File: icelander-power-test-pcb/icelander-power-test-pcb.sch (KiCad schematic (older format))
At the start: 24 parts

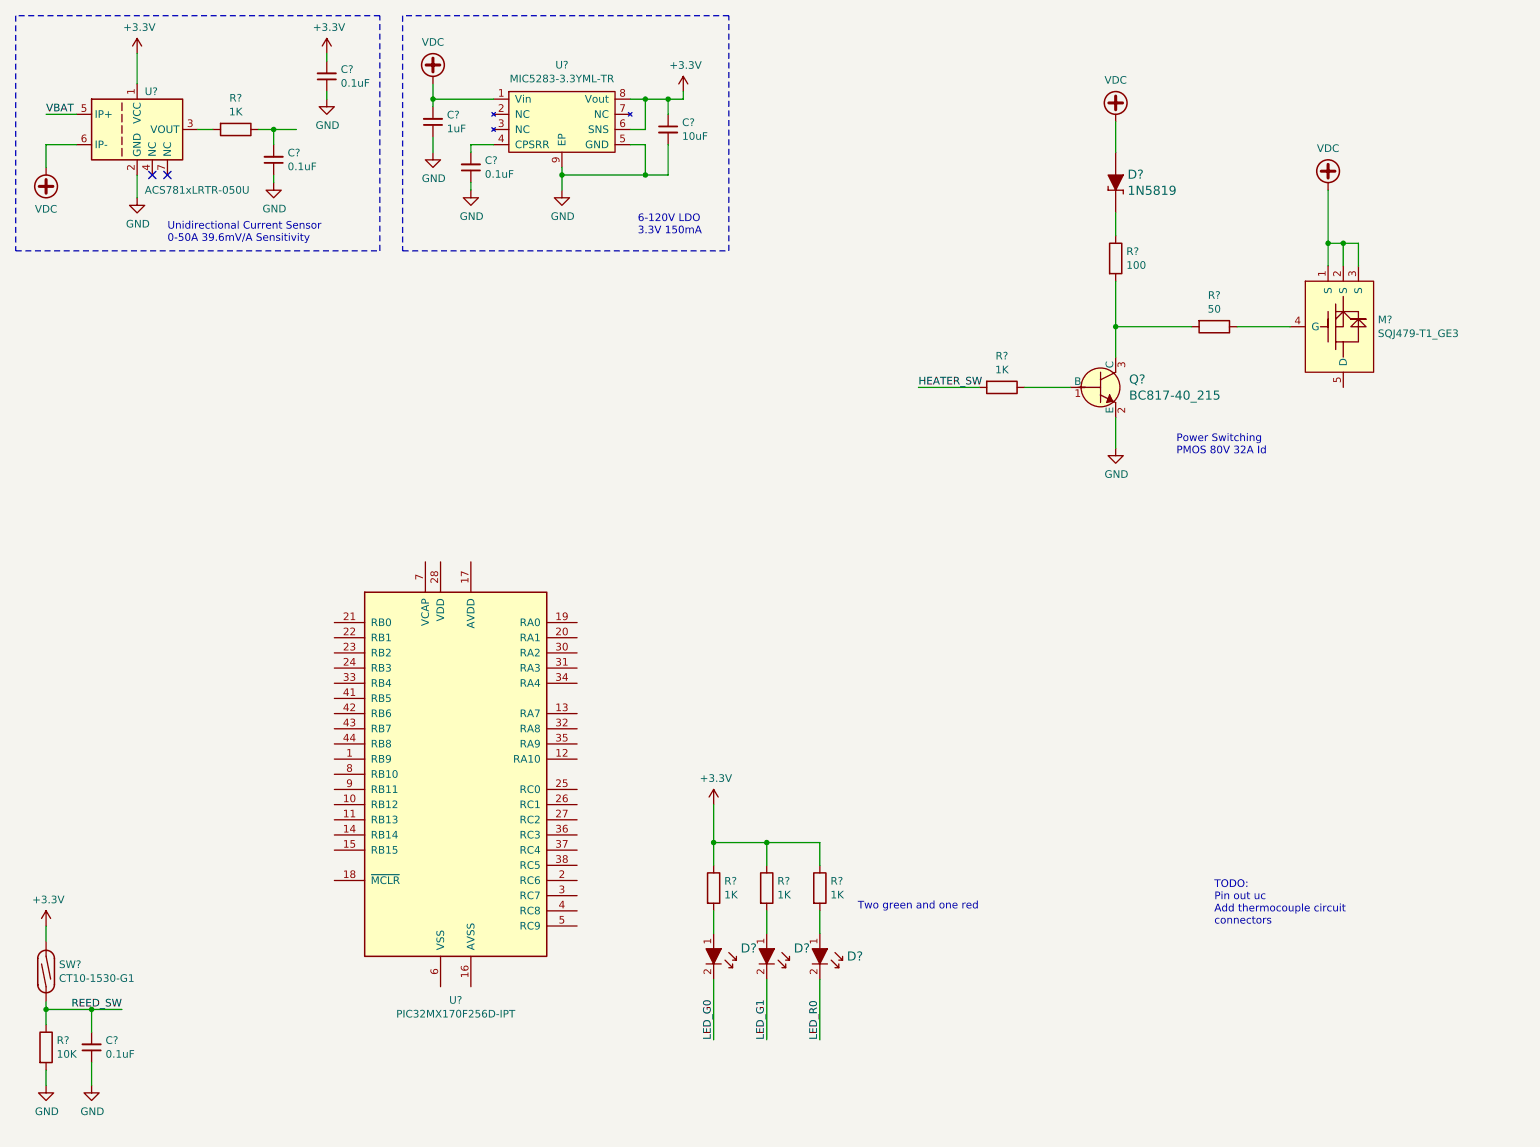
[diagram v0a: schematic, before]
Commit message: soft schematic finished
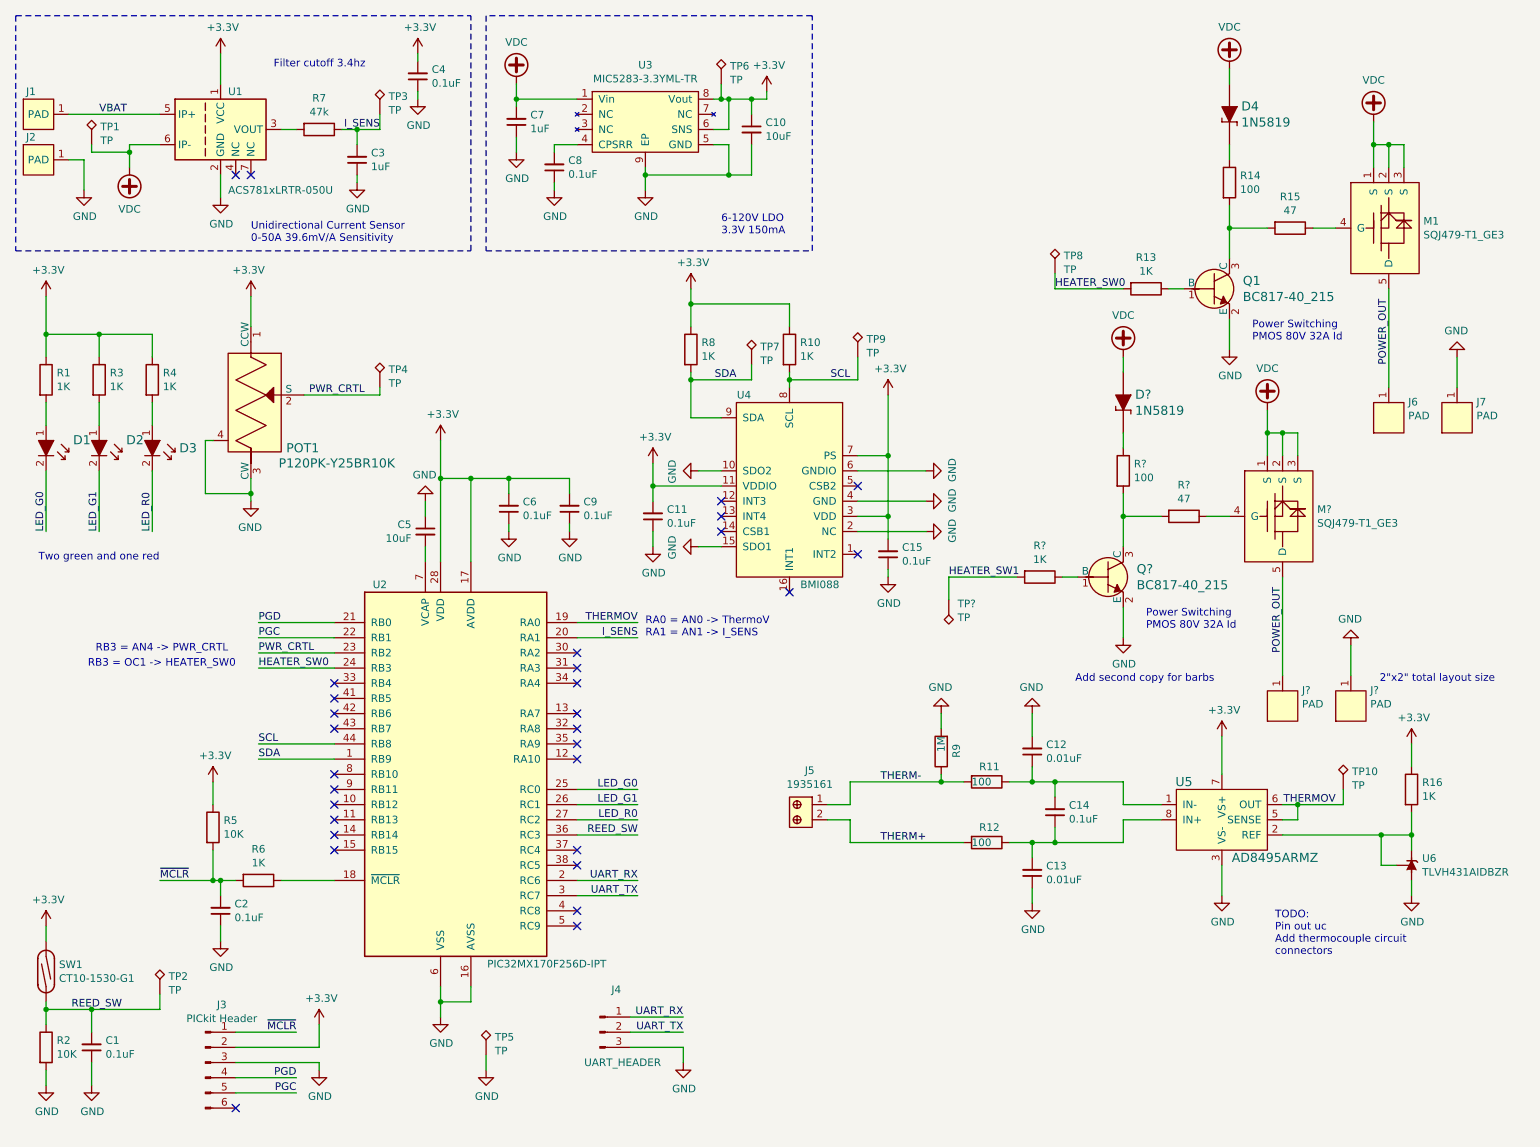
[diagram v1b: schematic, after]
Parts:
- removed C?: 0.1uF, Capacitor_SMD:C_0805_2012Metric_Pad1.15x1.40mm_HandSolder, symbol Device:C_Small
- added C11, C14, C15, C2, C6, C9: 0.1uF, Capacitor_SMD:C_0805_2012Metric_Pad1.15x1.40mm_HandSolder, symbol Device:C_Small
- added C12, C13: 0.01uF, Capacitor_SMD:C_0805_2012Metric_Pad1.15x1.40mm_HandSolder, symbol Device:C_Small
- added C3: 1uF, Capacitor_SMD:C_0805_2012Metric_Pad1.15x1.40mm_HandSolder, symbol Device:C_Small
- added C5: 10uF, Capacitor_SMD:C_0805_2012Metric_Pad1.15x1.40mm_HandSolder, symbol Device:C_Small
- added D?: 1N5819, digikey-footprints:DO-41, symbol dk_Diodes-Rectifiers-Single:1N5819
- added J1, J2, J6, J7, J? (x2): PAD, icelander-power-test-pcb:PowerPad, symbol IceLander-Power-test-pcb:PAD
- added J3: PICkit Header, Connector_PinHeader_2.54mm:PinHeader_1x06_P2.54mm_Vertical, symbol Connector:Conn_01x06_Male
- added J4: UART_HEADER, Connector_PinHeader_2.54mm:PinHeader_1x03_P2.54mm_Vertical, symbol Connector:Conn_01x03_Male
- added J5: 1935161, digikey-footprints:Terminal_Block_D1.3mm_P5mm, symbol dk_Terminal-Blocks-Wire-to-Board:1935161
- added M?: SQJ479-T1_GE3, Package_SO:PowerPAK_SO-8_Single, symbol IceLander-Power-test-pcb:SQJ479-T1_GE3
- added POT1: P120PK-Y25BR10K, digikey-footprints:Potentiometer_P120PK-Y25BR10K, symbol dk_Rotary-Potentiometers-Rheostats:P120PK-Y25BR10K
- added Q?: BC817-40_215, digikey-footprints:SOT-23-3, symbol dk_Transistors-Bipolar-BJT-Single:BC817-40_215
- added R10, R16, R6, R8, R?: 1K, Resistor_SMD:R_0805_2012Metric_Pad1.15x1.40mm_HandSolder, symbol Device:R
- added R11, R12, R?: 100, Resistor_SMD:R_0805_2012Metric_Pad1.15x1.40mm_HandSolder, symbol Device:R
- added R5: 10K, Resistor_SMD:R_0805_2012Metric_Pad1.15x1.40mm_HandSolder, symbol Device:R
- added R9: 1M, Resistor_SMD:R_0805_2012Metric_Pad1.15x1.40mm_HandSolder, symbol Device:R
- added R?: 47, Resistor_SMD:R_0805_2012Metric_Pad1.15x1.40mm_HandSolder, symbol Device:R
- added TP1, TP10, TP2, TP3, TP4, TP5, TP6, TP7, TP8, TP9, TP?: TP, OSU_SIM_BASIC:Keystone_5019, symbol Connector:TestPoint_Alt
- added U4: BMI088, icelander-power-test-pcb:BMI088-LGA-16, symbol IceLander-Power-test-pcb:BMI088-Sensor_Motion
- added U5: AD8495ARMZ, digikey-footprints:TSSOP-8_W3mm, symbol dk_Interface-Sensor-and-Detector-Interfaces:AD8495ARMZ
- added U6: TLVH431AIDBZR, Package_TO_SOT_SMD:SOT-23, symbol Reference_Voltage:TL431DBZ
- C1, C4, C8: renamed from C?; Digi-Key_PN (none) -> 399-8000-1-ND
- C10: renamed from C?; Digi-Key_PN (none) -> 1276-2893-1-ND
- C7: renamed from C?; Digi-Key_PN (none) -> 399-1284-1-ND
- R1, R13, R3, R4: renamed from R?; Digi-Key_PN (none) -> 311-1.0KARCT-ND
- R14: renamed from R?; Digi-Key_PN (none) -> P100DACT-ND
- R15: renamed from R?; value 50 -> 47; Digi-Key_PN (none) -> A126371CT-ND
- R2: renamed from R?; Digi-Key_PN (none) -> 311-10.0KCRCT-ND
- R7: renamed from R?; value 1K -> 47k; Digi-Key_PN (none) -> A130144CT-ND
- SW1: renamed from SW?; footprint (none) -> icelander-power-test-pcb:CT10-XXXX-G1
- gave numbers to parts that had none: 9
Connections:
- net HEATER_SW is gone; now on net HEATER_SW0: R13.2
- net +3V3: now also U2.17 (AVDD), U2.28 (VDD), U2.40 (VDD), C11.2, C15.2, C6.2, C9.2, J3.2 (Pin_2), POT1.1 (CCW), R10.1, R16.1, R5.1, R8.1, TP6.1, U4.11 (VDDIO), U4.3 (VDD), U4.7 (PS), U5.7 (VS+)
- net GND: now also U2.16 (AVSS), U2.29 (VSS), U2.39 (VSS), U2.6 (VSS), C11.1, C12.2, C13.1, C15.1, C2.1, C3.1, C5.1, C6.1, C9.1, J2.1, J3.3 (Pin_3), J4.3 (Pin_3), J7.1, J?.1, POT1.3 (CW), POT1.4, Q?.2 (E), R9.2, TP5.1, U4.10 (SDO2), U4.15 (SDO1), U4.2 (NC), U4.4 (GND), U4.6 (GNDIO), U5.3 (VS-), U6.3 (A)
- net LED_G0: now also U2.25 (RC0)
- net LED_G1: now also U2.26 (RC1)
- net LED_R0: now also U2.27 (RC2)
- net REED_SW: now also U2.36 (RC3), TP2.1
- net VBAT: now also J1.1
- net VDC: now also D?.A, M?.1 (S), M?.2 (S), M?.3 (S), TP1.1
- net POWER_OUT: now reaches M1.5 (D)
- net POWER_OUT: now also J6.1, J?.1, M?.5 (D)
- net SDA: now reaches U2.1 (RB9)
- net SDA: now also R8.2, TP7.1, U4.9 (SDA)
- net at U2.18 (~MCLR): now also R6.1
- net THERMOV: now reaches U2.19 (RA0)
- net THERMOV: now also TP10.1, U5.5 (SENSE), U5.6 (OUT)
- net UART_RX: now reaches U2.2 (RC6)
- net UART_RX: now also J4.1 (Pin_1)
- net I_SENS: now reaches U2.20 (RA1)
- net I_SENS: now also R7.1, C3.2, TP3.1
- net PGD: now reaches U2.21 (RB0)
- net PGD: now also J3.4 (Pin_4)
- net PGC: now reaches U2.22 (RB1)
- net PGC: now also J3.5 (Pin_5)
- net PWR_CRTL: now reaches U2.23 (RB2)
- net PWR_CRTL: now also POT1.2 (S), TP4.1
- net HEATER_SW0: now reaches U2.24 (RB3)
- net HEATER_SW0: now also TP8.1
- net UART_TX: now reaches U2.3 (RC7)
- net UART_TX: now also J4.2 (Pin_2)
- net SCL: now reaches U2.44 (RB8)
- net SCL: now also R10.2, TP9.1, U4.8 (SCL)
- net at U2.7 (VCAP): now also C5.2
- new net: R16.2, U5.2 (REF), U6.1 (K), U6.2 (REF)
- new net: C12.1, C14.2, R11.1, U5.1 (IN-)
- new net: C13.2, C14.1, R12.1, U5.8 (IN+)
- new net: M?.4 (G), R?.1
- new net: Q?.1 (B), R?.1
- new net: Q?.3 (C), R?.2, R?.2
- new net: D?.K, R?.1
- new net HEATER_SW1: R?.2, TP?.1
- new net THERM+: J5.2, R12.2
- new net THERM-: J5.1, R11.2, R9.1
- new net ~MCLR: C2.2, J3.1 (Pin_1), R5.2, R6.2
- no-connect marks 2 -> 30
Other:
- note added: "2"x2" total layout size"
- note added: "Add second copy for barbs\n"
- note added: "Filter cutoff 3.4hz\n"
- note added: "RA0 = AN0 -> ThermoV\nRA1 = AN1 -> I_SENS"
- note added: "RB3 = AN4 -> PWR_CRTL"
- note added: "RB3 = OC1 -> HEATER_SW0\n"
- moved on the sheet: C10, C4, C7, C8, D1, D2, D3, D4, M1, Q1, R1, R13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

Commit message: sch finished ready to start layout
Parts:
- removed C10: 10uF, Capacitor_SMD:C_0805_2012Metric_Pad1.15x1.40mm_HandSolder, symbol Device:C_Small
- removed C3, C7: 1uF, Capacitor_SMD:C_0805_2012Metric_Pad1.15x1.40mm_HandSolder, symbol Device:C_Small
- removed C4, C8: 0.1uF, Capacitor_SMD:C_0805_2012Metric_Pad1.15x1.40mm_HandSolder, symbol Device:C_Small
- removed D4, D?: 1N5819, digikey-footprints:DO-41, symbol dk_Diodes-Rectifiers-Single:1N5819
- removed J1, J2, J6, J7, J? (x2): PAD, icelander-power-test-pcb:PowerPad, symbol IceLander-Power-test-pcb:PAD
- removed M1, M?: SQJ479-T1_GE3, Package_SO:PowerPAK_SO-8_Single, symbol IceLander-Power-test-pcb:SQJ479-T1_GE3
- removed Q1, Q?: BC817-40_215, digikey-footprints:SOT-23-3, symbol dk_Transistors-Bipolar-BJT-Single:BC817-40_215
- removed R13, R?: 1K, Resistor_SMD:R_0805_2012Metric_Pad1.15x1.40mm_HandSolder, symbol Device:R
- removed R14, R?: 100, Resistor_SMD:R_0805_2012Metric_Pad1.15x1.40mm_HandSolder, symbol Device:R
- removed R15, R?: 47, Resistor_SMD:R_0805_2012Metric_Pad1.15x1.40mm_HandSolder, symbol Device:R
- removed R7: 47k, Resistor_SMD:R_0805_2012Metric_Pad1.15x1.40mm_HandSolder, symbol Device:R
- removed TP1, TP3, TP6, TP8, TP?: TP, OSU_SIM_BASIC:Keystone_5019, symbol Connector:TestPoint_Alt
- removed U1: ACS781xLRTR-050U, Sensor_Current:Allegro_PSOF-7_4.8x6.4mm_P1.60mm, symbol Sensor_Current:ACS781xLRTR-050U
- removed U3: MIC5283-3.3YML-TR, icelander-power-test-pcb:VDFM-8_EP_3x3mm, symbol IceLander-Power-test-pcb:MIC5283-3.3YML-TR
- renumbered C14 to C10, C5 to C3, C11 to C4, C6 to C5, C9 to C6, C15 to C7, C12 to C8, C13 to C9, J3 to J1, J4 to J2, J5 to J3, R11 to R10, R12 to R11, R16 to R12, R8 to R7, R10 to R8, TP2 to TP1, TP4 to TP2, TP5 to TP3, TP7 to TP4, TP9 to TP5, TP10 to TP6, U2 to U1, U4 to U2, U5 to U3, U6 to U4
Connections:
- net HEATER_SW1: now also U1.41 (RB5)
- net PGOOD: now reaches U1.37 (RC4)
- no-connect marks 30 -> 26
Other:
- note added: "DC Regulation\nPower Switching\nPower Monitoring"
- note added: "RB5 = OC2 -> HEATER_SW1\n"
- note removed: "6-120V LDO\n3.3V 150mA"
- note removed: "Add second copy for barbs\n"
- note removed: "Filter cutoff 3.4hz\n"
- note removed: "Power Switching \nPMOS 80V 32A Id"
- note removed: "Unidirectional Current Sensor\n0-50A 39.6mV/A Sensitivity"
- moved on the sheet: C4, C7, D1, D2, D3, POT1, R1, R3, R4, R7, R8, TP2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

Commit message: swappe uc updated 3d settings
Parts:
- removed U1: PIC32MX170F256D-IPT, Package_QFP:TQFP-44_10x10mm_P0.8mm, symbol MCU_Microchip_PIC32:PIC32MX170F256D-IPT
- added C50, C51, C52, C53, C54, C55, C56: 0.1uF, Capacitor_SMD:C_0805_2012Metric_Pad1.15x1.40mm_HandSolder, symbol Device:C_Small
- added C57: 10uF, Capacitor_SMD:C_0805_2012Metric_Pad1.15x1.40mm_HandSolder, symbol Device:C_Small
- added FB1: BLM18PG121SN1D, Inductor_SMD:L_0603_1608Metric_Pad1.05x0.95mm_HandSolder, symbol dk_Ferrite-Beads-and-Chips:BLM18PG121SN1D
- added S1: GPTS203211B, digikey-footprints:PushButton_12x12mm_THT_GPTS203211B, symbol dk_Pushbutton-Switches:GPTS203211B
- added U1: STM32F030CCTx, Package_QFP:LQFP-48_7x7mm_P0.5mm, symbol MCU_ST_STM32F0:STM32F030CCTx
- added XTAL1: NX3225GD-8MHZ-STD-CRA-3, digikey-footprints:SMD-2_3.2x2.5mm, symbol dk_Crystals:NX3225GD-8MHZ-STD-CRA-3
- C3: value 10uF -> 10pF; Digi-Key_PN 1276-2893-1-ND -> 311-1058-1-ND
- C5: value 0.1uF -> 10pF; Digi-Key_PN 399-8000-1-ND -> 311-1058-1-ND
- J1: value PICkit Header -> SWIO Header
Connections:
- net +3V3: now also C50.2, C51.2, C52.2, C53.2, C54.2, C55.2, C56.2, C57.1, FB1.1, U1.1 (VDD), U1.24 (VDD), U1.36 (VDD), U1.48 (VDD); no longer C5.2, C6.2
- net GND: now also C50.1, C51.1, C52.1, C53.1, C54.1, C55.1, C56.1, C57.2, S1.2, U1.23 (VSS), U1.35 (VSS), U1.47 (VSS), U1.8 (VSSA)
- net HEATER_SW0: now also U1.29 (PA8)
- net HEATER_SW1: now also U1.30 (PA9)
- net I_SENS: now also U1.11 (PA1)
- net LED_G0: now also U1.13 (PA3)
- net LED_G1: now also U1.14 (PA4)
- net LED_R0: now also U1.15 (PA5)
- net PGOOD: now also U1.17 (PA7)
- net PWR_CRTL: now also U1.12 (PA2)
- net REED_SW: now also U1.16 (PA6)
- net SCL: now also U1.45 (PB8)
- net SDA: now also U1.43 (PB7)
- net THERMOV: now also U1.10 (PA0)
- net UART_RX: now also U1.31 (PA10)
- net UART_TX: now also U1.42 (PB6)
- net NRST: now reaches R6.1
- net NRST: now also J1.1 (Pin_1), U1.7 (NRST)
- net at C3.2: now also U1.5 (PF0), XTAL1.1
- net PGC renamed SWCLK
- net SWCLK: now also U1.37 (PA14)
- net PGD renamed SWDIO
- net SWDIO: now also U1.34 (PA13)
- net ~MCLR: no longer names the net of C2.2, R5.2, R6.2
- net ~MCLR: now also S1.1; no longer J1.1 (Pin_1)
- new net: C5.2, U1.6 (PF1), XTAL1.2
- new net: C6.2, FB1.2, U1.9 (VDDA)
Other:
- note added: "PA0 = AN0 -> ThermoV\nPA1 = AN1 -> I_SENS\nPA2 = AN2 -> PWR_CRTL"
- note removed: "RA0 = AN0 -> ThermoV\nRA1 = AN1 -> I_SENS"
- note removed: "RB3 = AN4 -> PWR_CRTL"
- note removed: "RB3 = OC1 -> HEATER_SW0\n"
- note removed: "RB5 = OC2 -> HEATER_SW1\n"
- moved on the sheet: C1, R2, SW1, TP1
